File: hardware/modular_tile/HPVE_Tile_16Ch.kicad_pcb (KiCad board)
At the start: 4 copper layers, 65 x 65 mm, 47 parts, among them U1 74HC595, U101 TC4427ACOA, U102 TC4427ACOA, U103 TC4427ACOA, U104 TC4427ACOA, U105 TC4427ACOA, U106 TC4427ACOA, U107 TC4427ACOA, U108 TC4427ACOA, U2 74HC595

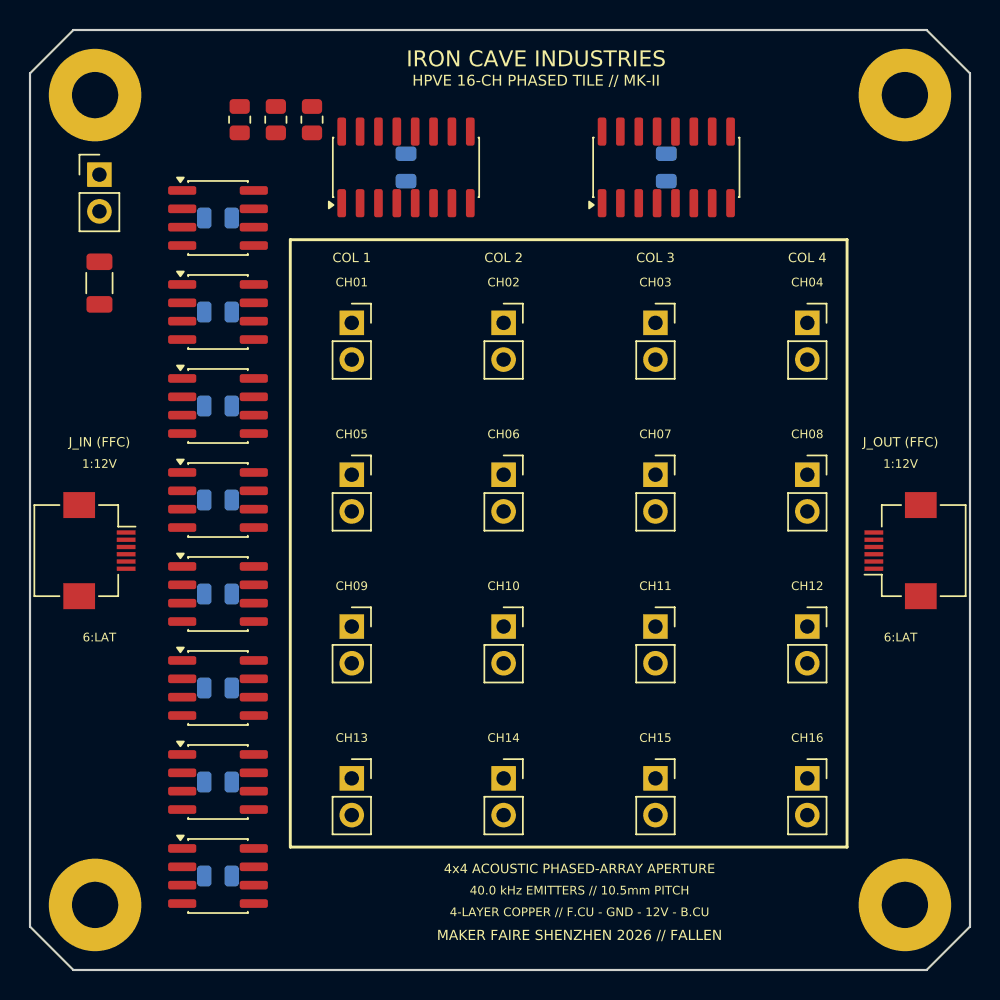
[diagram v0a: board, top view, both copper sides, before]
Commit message: docs(roadmap): update campaign roadmap to 216 XP, Stage 2 Sami evolution, and modular tile architecture
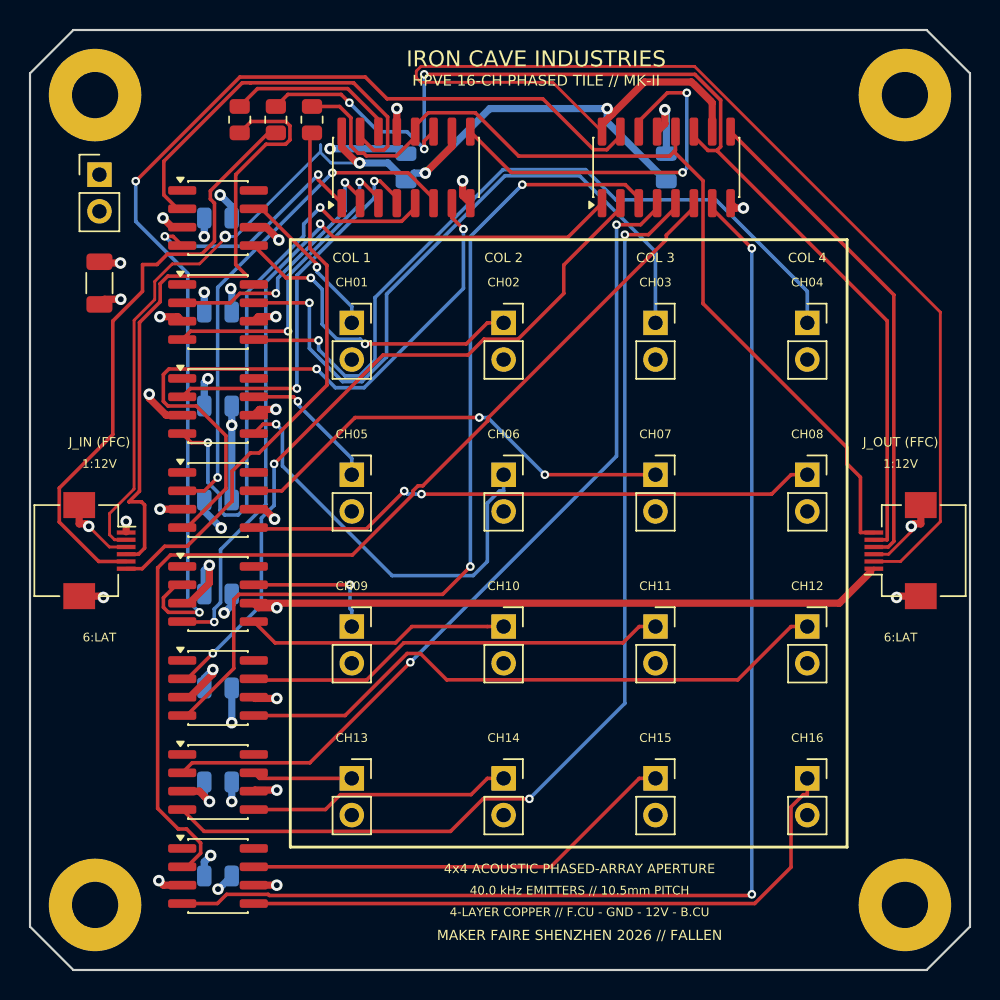
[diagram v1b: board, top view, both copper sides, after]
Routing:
- net +5V: track 0.00 -> 167.1 mm, vias 0 -> 4
- net SIG_16: track 0.00 -> 88.6 mm, vias 0 -> 2
- net SPI_SCK: track 0.00 -> 78.7 mm, vias 0 -> 3
- net +12V: track 0.00 -> 76.7 mm, vias 0 -> 17
- net SIG_9: track 0.00 -> 75.9 mm, vias 0 -> 2
- net SIG_14: track 0.00 -> 71.9 mm, vias 0 -> 2
- net SIG_15: track 0.00 -> 71.1 mm
- net SPI_LATCH: track 0.00 -> 64.7 mm
- net SIG_12: track 0.00 -> 63.7 mm, vias 0 -> 2
- net GND: track 0.00 -> 62.7 mm, vias 0 -> 23
- net SIG_13: track 0.00 -> 58.7 mm, vias 0 -> 2
- net DRV_4: track 0.00 -> 53.8 mm, vias 0 -> 1
- net SIG_10: track 0.00 -> 53.7 mm, vias 0 -> 2
- net SIG_11: track 0.00 -> 50.5 mm, vias 0 -> 2
- net DRV_3: track 0.00 -> 47.4 mm, vias 0 -> 1
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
